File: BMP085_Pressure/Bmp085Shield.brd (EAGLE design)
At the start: 39.7 x 26.7 mm, 5 parts

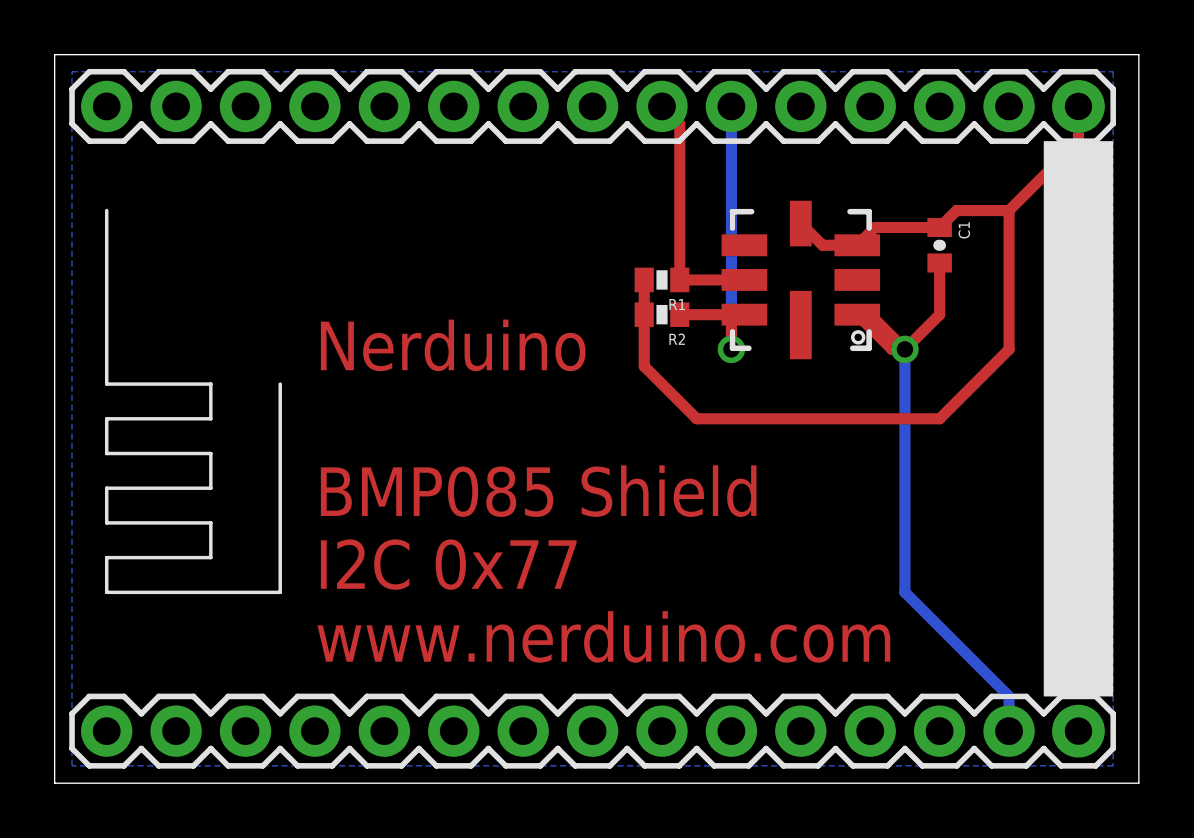
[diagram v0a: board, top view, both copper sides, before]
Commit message: Updated stencil text Added PCA9685 and ITG3200 shields
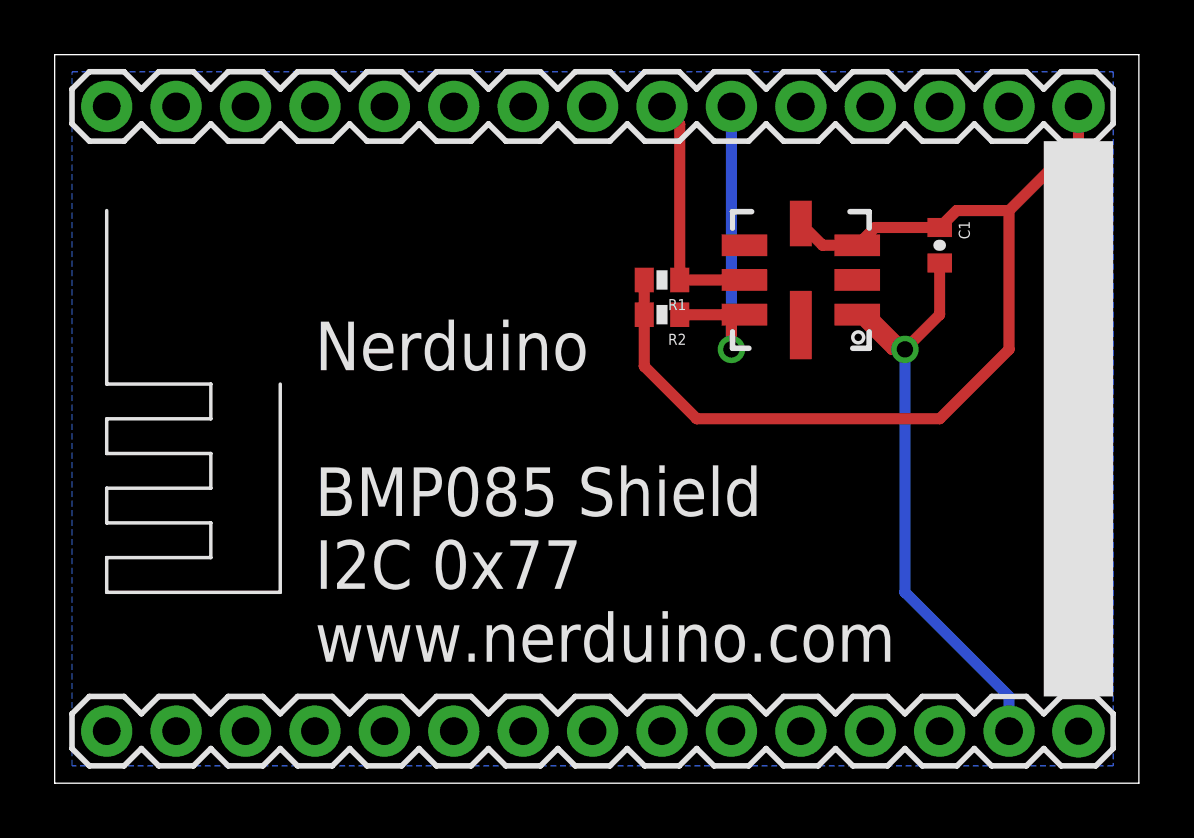
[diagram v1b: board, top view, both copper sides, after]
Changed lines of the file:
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@@
 <wire x1="39.04" y1="26.025" x2="-0.635" y2="26.025" width="0" layer="20"/>
 <wire x1="-0.635" y1="26.025" x2="-0.635" y2="-0.635" width="0" layer="20"/>
-<text x="8.89" y="3.81" size="1.778" layer="1">Nerduino
+<text x="8.89" y="3.81" size="1.778" layer="121">Nerduino
 BMP085 Shield
 I2C 0x77
